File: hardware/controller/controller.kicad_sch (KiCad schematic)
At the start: 194 parts, among them J1 Conn_01x05, J2 Conn_01x03, J3 Conn_01x04, J4 USB_B_Micro, J5 Conn_01x03, J6 Conn_01x02, Q1 MMBT2222A 1P, Q2 AO3400A, SW1 ILS_TA180_50, SW10 SW_Push, SW11 SW_SPDT, SW2 ILS_TA180_50, SW3 ILS_TA180_50, SW4 ILS_TA180_50, SW5 ILS_TA180_50, SW6 ILS_TA180_50, SW7 ILS_TA180_50, SW8 ILS_TA180_50, SW9 ILS_TA180_50, U1 WS2811, U10 CH340X, U2 FM24CL16B, U3 WS2811, U4 WS2811, U5 HT75xx-1-SOT89, U6 RFM69CW-915MHZ, U7 TP4056, U8 STM32G070CBTx, U9 ISL29125

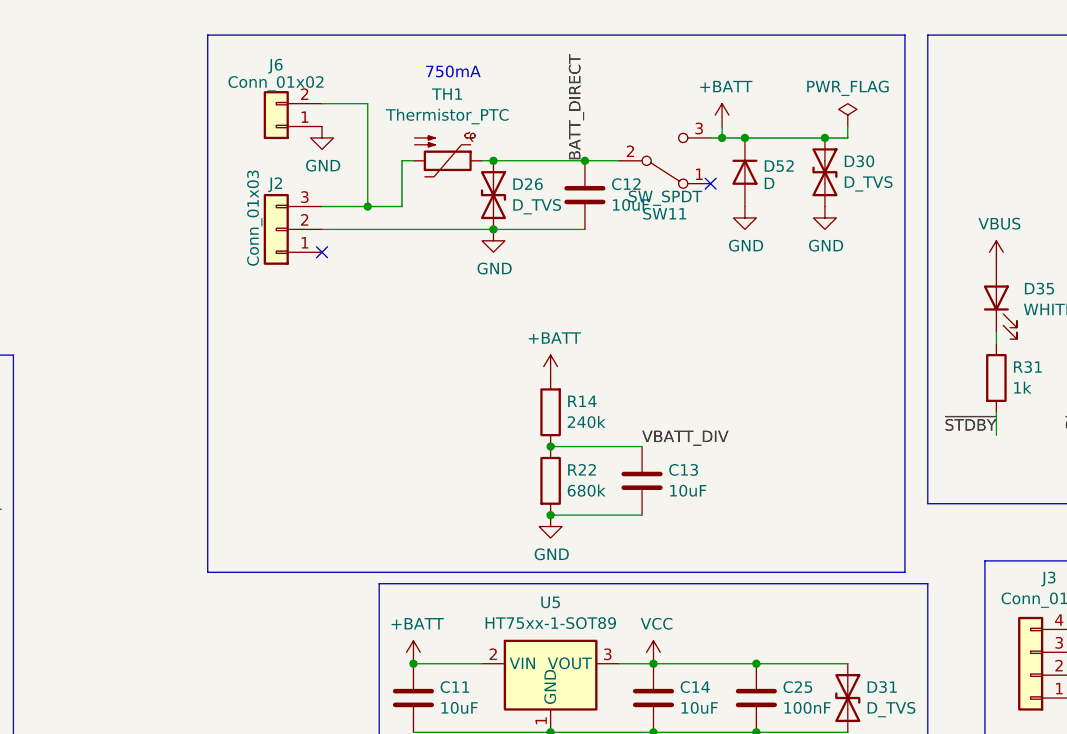
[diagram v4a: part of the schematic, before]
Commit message: Controller v1.1 updates:
- Move crowbar diode before the switch
- Change to in-stock TVS diodes

Change-Id: I54c2ed7b3562a7853553227b0bcbf77bde420927
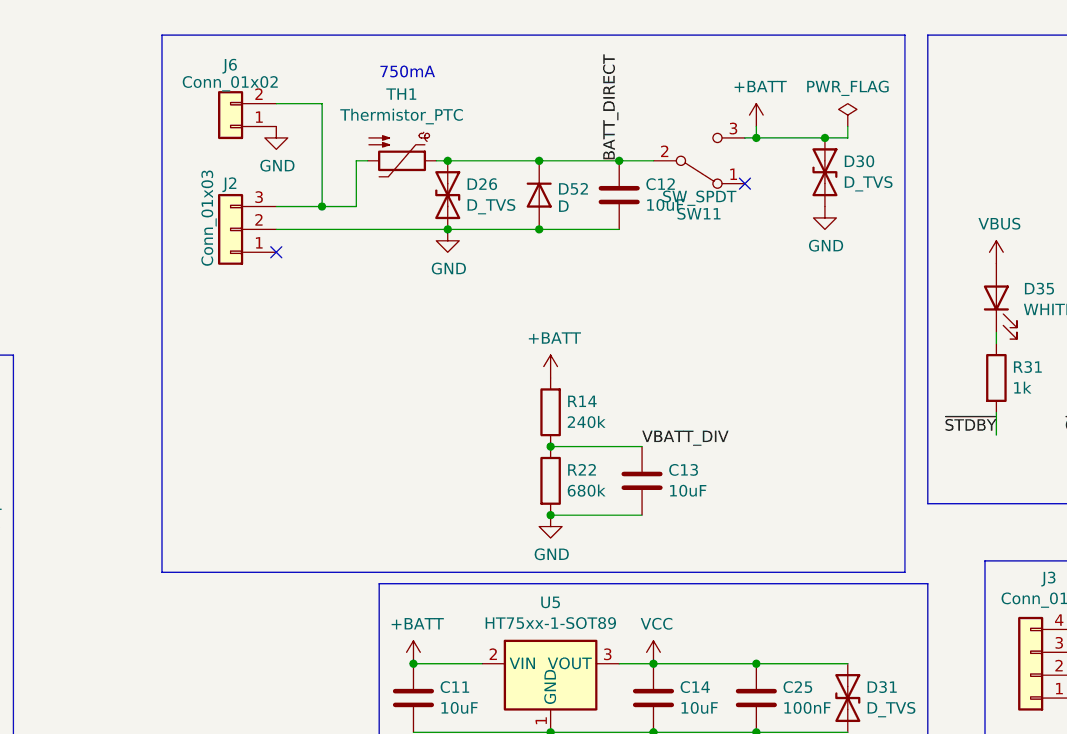
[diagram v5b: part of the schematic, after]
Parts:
- D1, D2, D26, D30, D31, D4, D50, D51, D53, D54, D55, D56, D57: footprint Diode_SMD:D_SOD-323 -> Diode_SMD:D_SOD-123F; LCSC C127522 -> C2990473
- J4: footprint homebrew:FRAMATOME_10118194-0001LF_fixed_bridges -> Homebrew:FRAMATOME_10118194-0001LF_fixed_bridges
- S1: footprint OS102011MS8QP1 -> Homebrew:OS102011MS8QP1
- U6: footprint RFM69CW-XXXS2 -> Homebrew:RFM69CW-minimalpads
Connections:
- net +BATT: no longer D52.1 (K)
- net BATT_DIRECT: now also D52.1 (K)
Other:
- moved on the sheet: C12, D26, D52, J2, J6, SW11, TH1

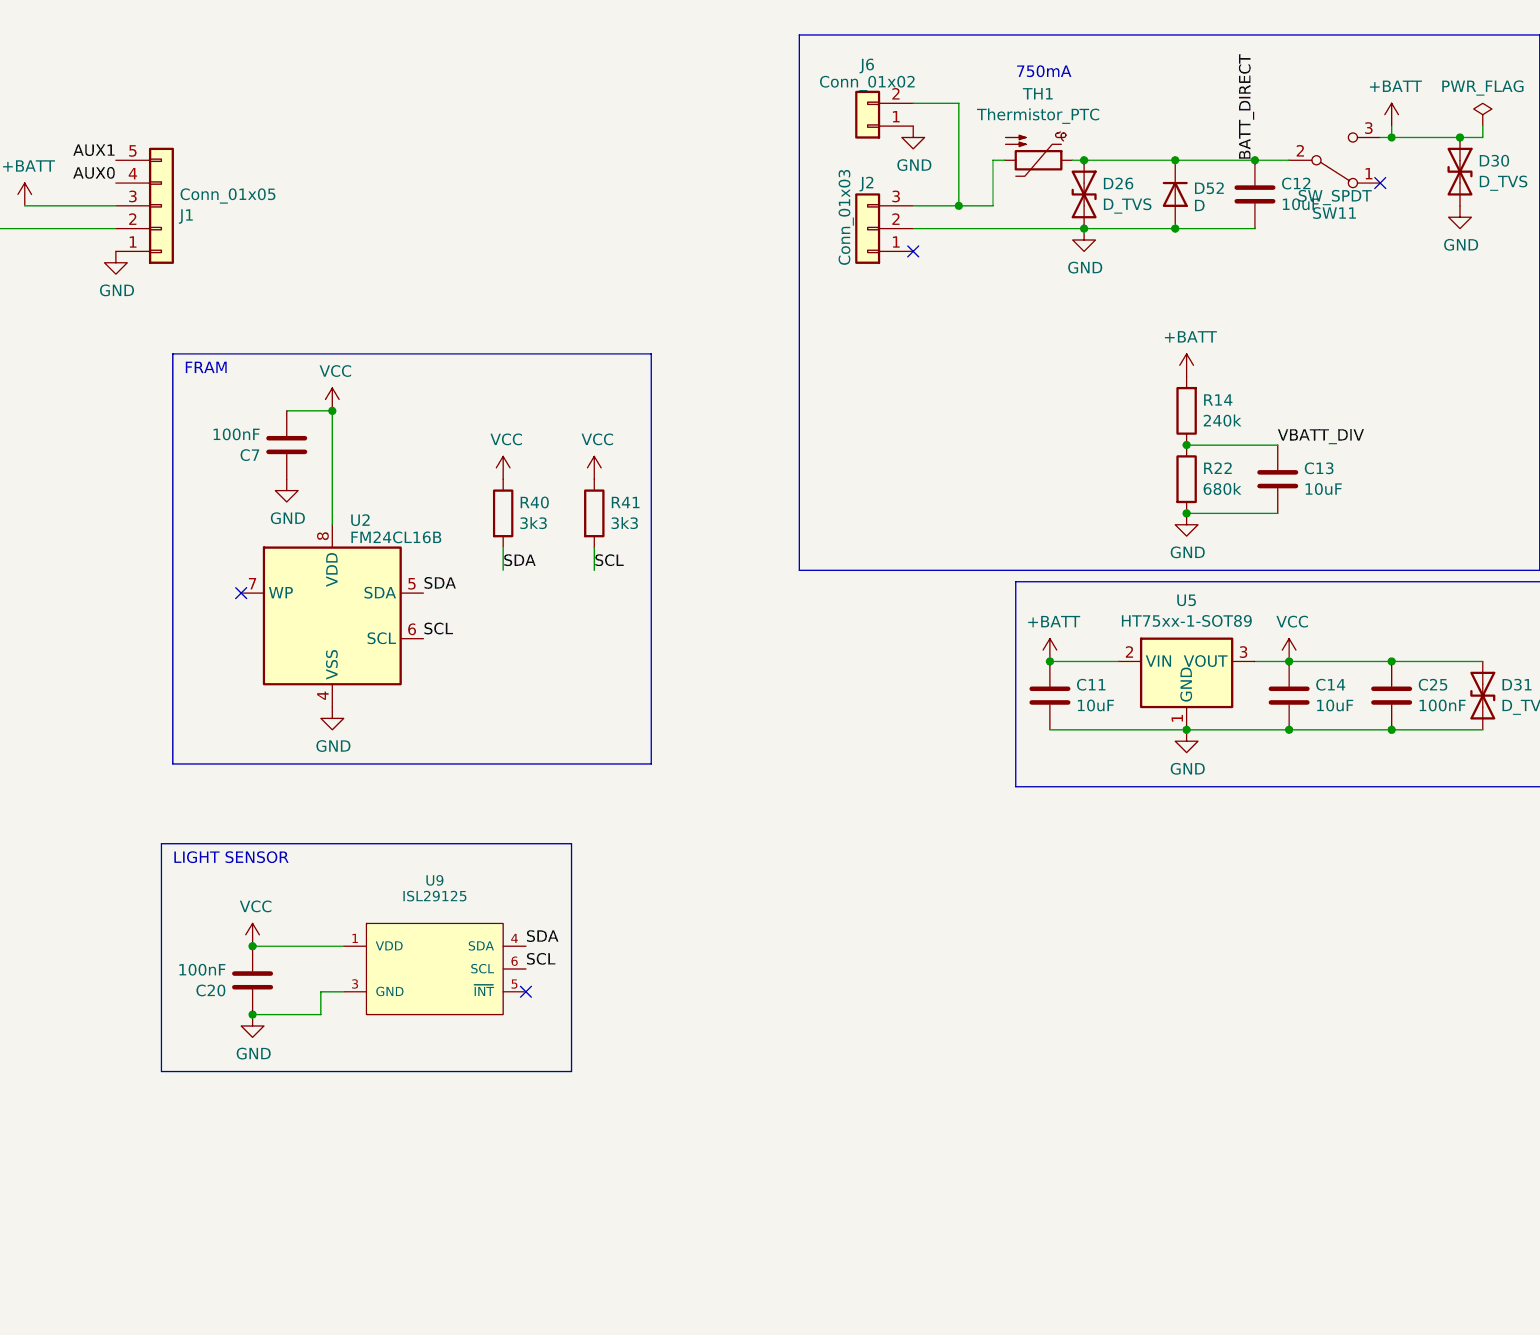
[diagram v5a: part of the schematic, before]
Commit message: Update controller PCB v1.1:
- Switch to in-stock light sensor
- Move power switch to top of board, so it's populated by JLC

Change-Id: I8973979a1cd224c9d926090501cf37b5c34c39ea
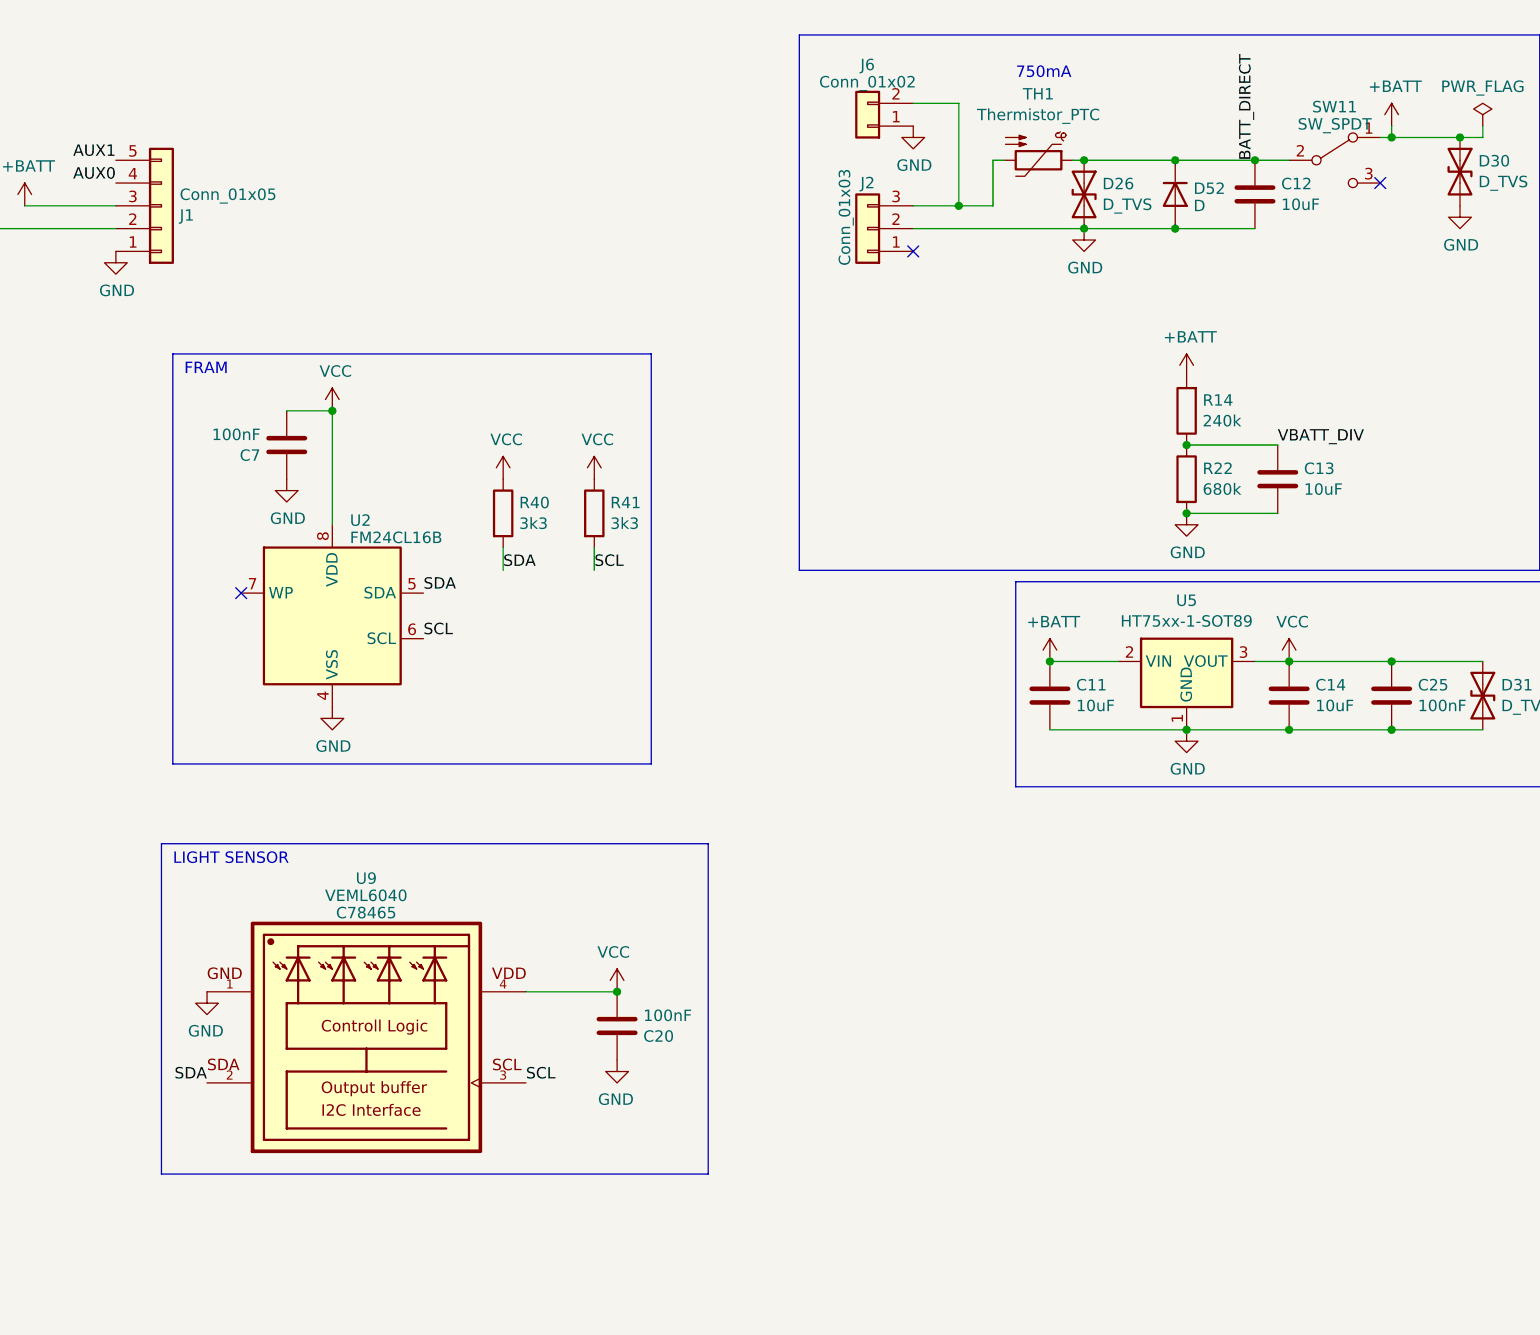
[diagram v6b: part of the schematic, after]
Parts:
- removed U9: ISL29125, Sparkfun_Silicon_Standard:ODFN-6, symbol SparkFun_Sensors:ISL29125
- added U9: VEML6040, Homebrew:VISHAY_VEML6040_1.25X2X1, symbol Homebrew:VEML6040
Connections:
- net +BATT: now also SW11.1 (A); no longer SW11.3 (C)
- net GND: now also U9.1
- net SCL: now also U9.3
- net SDA: now also U9.2
- net VCC: now also U9.4
- no-connect marks 52 -> 51
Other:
- moved on the sheet: C20

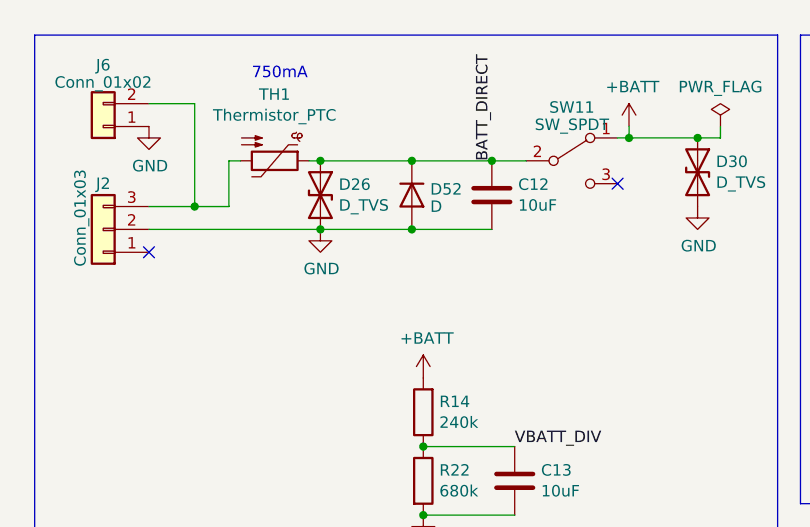
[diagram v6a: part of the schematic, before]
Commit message: Update schematic for fancy-node v1.2, and first pass at layout:
- Smaller buttons
- Smaller PCB antenna
- Smaller power switch
- Move to CH340X, hook up BOOT0 to it
- Smaller overall board size (47mm x 33mm, vs 60mm x 37mm)
- Add JST 1.25 for batteries
- Add crowbar diode for reverse polarity protection

Change-Id: I9a7a19972de9e62944e1a6f148661a5dd9e6b807
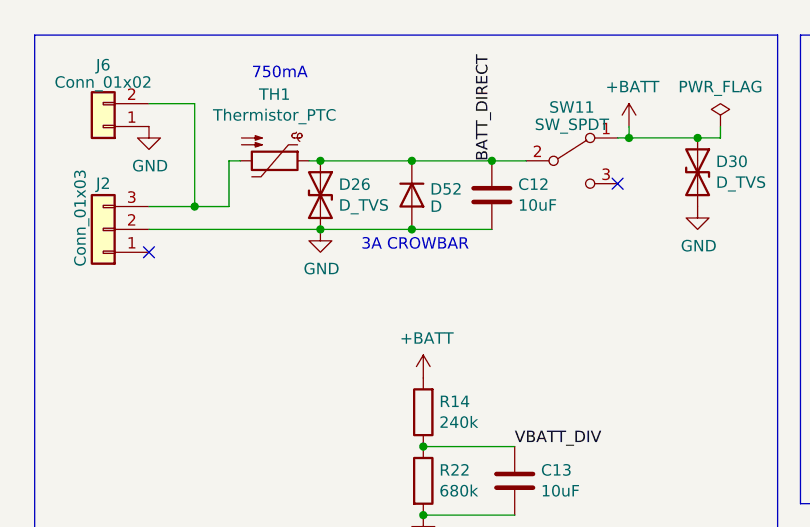
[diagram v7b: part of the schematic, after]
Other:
- note added: "3A CROWBAR"
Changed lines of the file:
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@@
     (effects (font (size 1.27 1.27)) (justify left bottom))
+  )
+  (text "3A CROWBAR" (at 269.24 38.1 0)
+    (effects (font (size 1.27 1.27)) (justify right bottom))
   )
   (text "FRAM" (at 152.4 52.07 0)
